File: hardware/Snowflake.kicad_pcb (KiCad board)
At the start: 2 copper layers, 58 parts, among them U1 556, U2 Mux_1_of_8

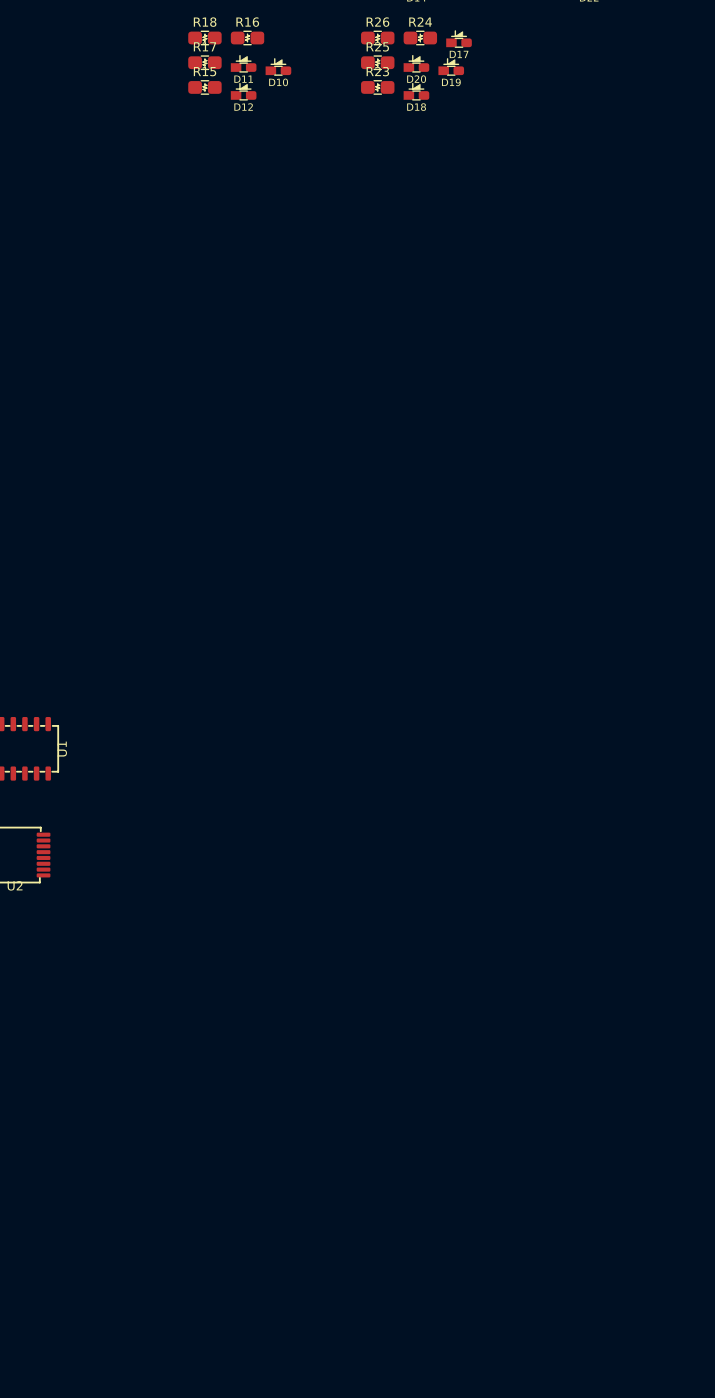
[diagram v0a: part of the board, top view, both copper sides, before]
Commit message: Added the Snowflake part to the library
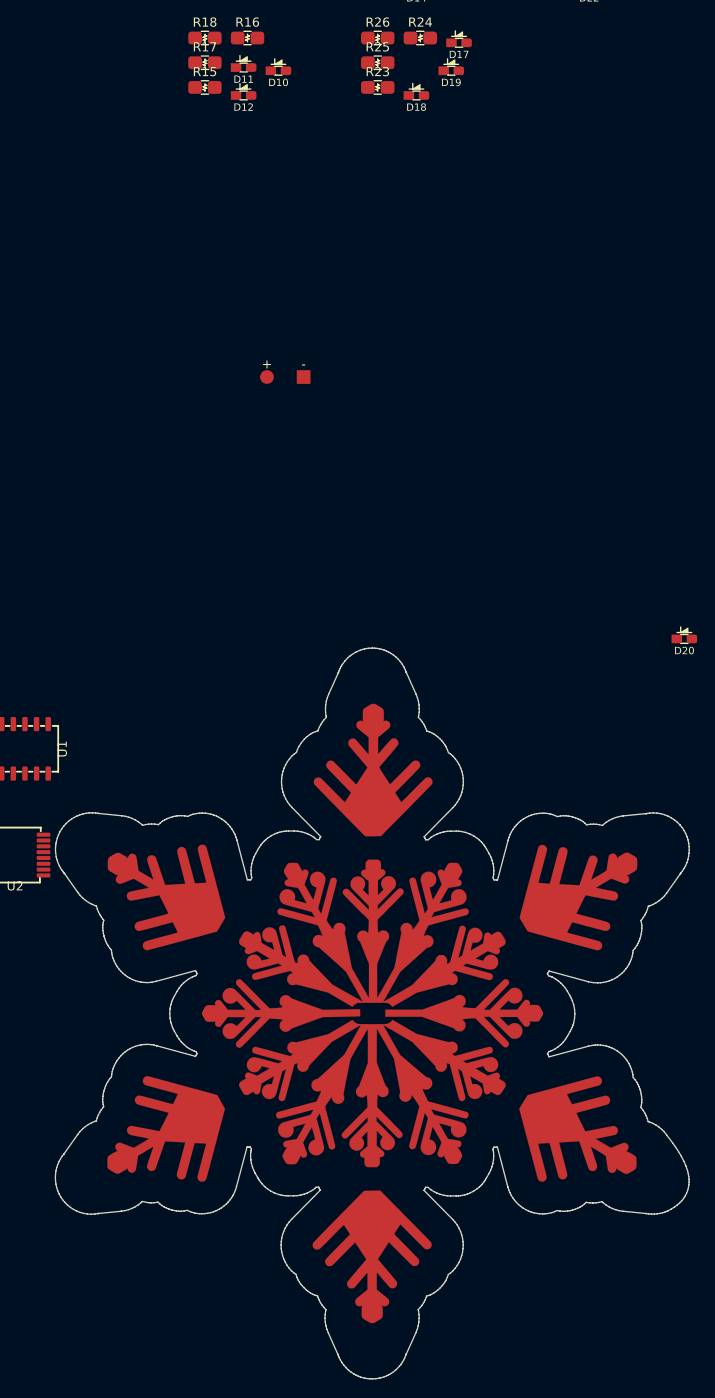
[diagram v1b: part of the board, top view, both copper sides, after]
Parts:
- added REF**: Battery_Holder-AAA, Snowflake:Battery_Holder-AAA, F.Cu at (119.8, 23.5)
- added Ref**: Val**, SnowFlake_1:Proto1, F.Cu at (129.3, 93.0)
- moved D20 68.9 mm to (163.4, 52.1)
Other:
- board outline added: 69.2 x 79.8 mm

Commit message: Schematic 99%, just needs a couple of tweaks (assign footprints to the OpAmp and the switch) Added a bunch of 3D models and footprints
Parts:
- removed C1, C2: C_Small, Snowflake:0805-C_Handsolder
- removed D1, D10, D11, D12, D13, D14, D15, D16, D17, D18, D19, D2, D20, D21, D22, D23, D24, D3, D4, D5, D6, D7, D8, D9: White, Snowflake:0603_LED_HandSolder
- removed R1, R2, R3, R4, R5, R6: R_Small, Snowflake:0805-R_Handsolder
- removed R10, R11, R12, R13, R14, R15, R16, R17, R18, R19, R20, R21, R22, R23, R24, R25, R26, R27, R28, R29, R30, R7, R8, R9: XYZΩ, Snowflake:0805-R_Handsolder
- removed REF**: Battery_Holder-AAA, Snowflake:Battery_Holder-AAA
- removed Ref**: Val**, SnowFlake_1:Proto1
- removed U1: 556, Snowflake:14-SOIC_4x8.75mm_.5-NA556
- removed U2: Mux_1_of_8, Snowflake:16-TSSOP_5x6.5mm_P0.65-MUX
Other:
- board outline removed

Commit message: Terayza new parts added and some layout started
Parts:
- added BT1: Battery, Snowflake:Battery_Holder-AAA, B.Cu at (206.8, 96.4)
- added C1: C_Small, Snowflake:0805-C_Handsolder, B.Cu at (162.0, 100.5)
- added D1: White, Snowflake:0603_LED_HandSolder, F.Cu at (108.6, 76.9)
- added D10: White, Snowflake:0603_LED_HandSolder, F.Cu at (138.2, 112.5)
- added D13: White, Snowflake:0603_LED_HandSolder, F.Cu at (108.5, 113.0)
- added D14: White, Snowflake:0603_LED_HandSolder, F.Cu at (108.5, 129.9)
- added D17: White, Snowflake:0603_LED_HandSolder, F.Cu at (93.1, 103.9)
- added D18: White, Snowflake:0603_LED_HandSolder, F.Cu at (78.8, 112.4)
- added D2: White, Snowflake:0603_LED_HandSolder, F.Cu at (108.5, 59.9)
- added D21: White, Snowflake:0603_LED_HandSolder, F.Cu at (92.5, 85.3)
- added D22: White, Snowflake:0603_LED_HandSolder, F.Cu at (77.6, 76.8)
- added D3: White, Snowflake:0603_LED_HandSolder, F.Cu at (108.5, 94.9)
- added D5: White, Snowflake:0603_LED_HandSolder, F.Cu at (123.9, 85.9)
- added D6: White, Snowflake:0603_LED_HandSolder, F.Cu at (138.4, 77.3)
- added D9: White, Snowflake:0603_LED_HandSolder, F.Cu at (123.7, 104.1)
- added Logo1: Snowflake, Snowflake:Snowflake, F.Cu at (108.5, 94.9)
- added R1: 50kΩ, Snowflake:0805-R_Handsolder, B.Cu at (159.4, 100.5)
- added R11: XYZΩ, Snowflake:0805-R_Handsolder, B.Cu at (139.5, 95.6)
- added R12: XYZΩ, Snowflake:0805-R_Handsolder, B.Cu at (143.5, 94.1)
- added R15: XYZΩ, Snowflake:0805-R_Handsolder, B.Cu at (123.1, 122.5)
- added R16: XYZΩ, Snowflake:0805-R_Handsolder, B.Cu at (126.4, 125.3)
- added R19: XYZΩ, Snowflake:0805-R_Handsolder, B.Cu at (92.2, 121.9)
- added R2: 35kΩ, Snowflake:0805-R_Handsolder, B.Cu at (156.1, 107.0)
- added R20: XYZΩ, Snowflake:0805-R_Handsolder, B.Cu at (91.5, 126.1)
- added R23: XYZΩ, Snowflake:0805-R_Handsolder, B.Cu at (76.9, 94.7)
- added R24: XYZΩ, Snowflake:0805-R_Handsolder, B.Cu at (72.9, 96.1)
- added R27: XYZΩ, Snowflake:0805-R_Handsolder, B.Cu at (93.1, 67.0)
- added R28: XYZΩ, Snowflake:0805-R_Handsolder, B.Cu at (89.8, 64.2)
- added R3: 30kΩ, Snowflake:0805-R_Handsolder, B.Cu at (166.6, 109.0)
- added R4: XYZΩ, Snowflake:0805-R_Handsolder, B.Cu at (163.0, 74.2)
- added R7: XYZΩ, Snowflake:0805-R_Handsolder, B.Cu at (124.8, 68.2)
- added R8: XYZΩ, Snowflake:0805-R_Handsolder, B.Cu at (125.5, 64.0)
- added RV1: 200kΩ, Snowflake:Potentiometer_TC33X-2-204E, B.Cu at (166.4, 104.2)
- added SW1: SW_SPST, Snowflake:Slide_Switch_JS202011SCQN, B.Cu at (167.8, 87.5)
- added U1: Opamp_Single, Snowflake:Op_Amp_SOT23_MCP6001T, B.Cu at (160.8, 107.5)
- added U2: 74HC595, Snowflake:16-TSSOP_5x6.5mm_P0.65-74HC565, B.Cu at (171.7, 76.1)
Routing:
- net Net-(R1-Pad2): track 0.00 -> 12.5 mm
- net Net-(R2-Pad2): track 0.00 -> 11.0 mm
- net CLK: track 0.00 -> 8.30 mm
- net Net-(C1-Pad1): track 0.00 -> 8.13 mm
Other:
- board outline added: 70.5 x 79.8 mm

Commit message: Terayza changes
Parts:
- added R5: 6.8kΩ, Snowflake:0805-R_Handsolder, B.Cu at (65.0, 96.1)
- added U3: LM4041_1.2V, Snowflake:SOT-23_LM4041_1.2V_Handsolder, B.Cu at (69.0, 97.2)
- moved U2 124.3 mm to (49.4, 98.2)
- moved R3 105.2 mm to (62.1, 96.1), turned to 90 degrees
- moved U1 103.5 mm to (57.6, 98.8)
- moved R1 102.3 mm to (57.5, 91.3), turned to 0 degrees
- moved RV1 100.8 mm to (66.4, 91.3), turned to 270 degrees
- moved R2 99.4 mm to (57.5, 94.0), turned to 0 degrees
- moved C1 88.5 mm to (73.6, 96.0)
- moved R4 53.4 mm to (113.8, 95.0), turned to 180 degrees
- moved SW1 22.0 mm to (152.2, 103.2)
- moved BT1 20.9 mm to (186.1, 99.3)
- moved R27 17.7 mm to (89.8, 84.3), turned to 150 degrees
- moved R15 17.3 mm to (127.2, 105.7), turned to 330 degrees
- moved R12 17.2 mm to (135.1, 79.2), turned to 210 degrees
- moved R28 17.1 mm to (81.7, 79.3), turned to 330 degrees
- moved R23 17.1 mm to (90.0, 105.8), turned to 210 degrees
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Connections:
- C1 pad 2: GND -> VBIAS
- R11 pad 2: GND -> /Stem 2/VK
- R12 pad 2: GND -> /Stem 2/VK
- R15 pad 2: GND -> /Stem 3/VK
- R16 pad 2: GND -> /Stem 3/VK
- R19 pad 2: GND -> /Stem 4/VK
- R20 pad 2: GND -> /Stem 4/VK
- R23 pad 2: GND -> /Stem 5/VK
- R24 pad 2: GND -> /Stem 5/VK
- R27 pad 2: GND -> /Stem 6/VK
- R28 pad 2: GND -> /Stem 6/VK
- R3 pad 2: GND -> VBIAS
- R7 pad 2: GND -> /Led Stem 1/VK
- R8 pad 2: GND -> /Led Stem 1/VK
- U1 pad 3: Net-(C1-Pad1) -> Net-(R2-Pad2)
- U1 pad 4: Net-(R2-Pad2) -> Net-(C1-Pad1)
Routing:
- net Net-(C1-Pad1): track 8.13 -> 30.8 mm
- net VBIAS: track 0.00 -> 13.0 mm
- net Net-(R1-Pad2): track 12.5 -> 6.22 mm
- net VBAT: track 0.00 -> 4.28 mm
- net Net-(R2-Pad2): track 11.0 -> 6.77 mm
- net CLK: track 8.30 -> 10.9 mm

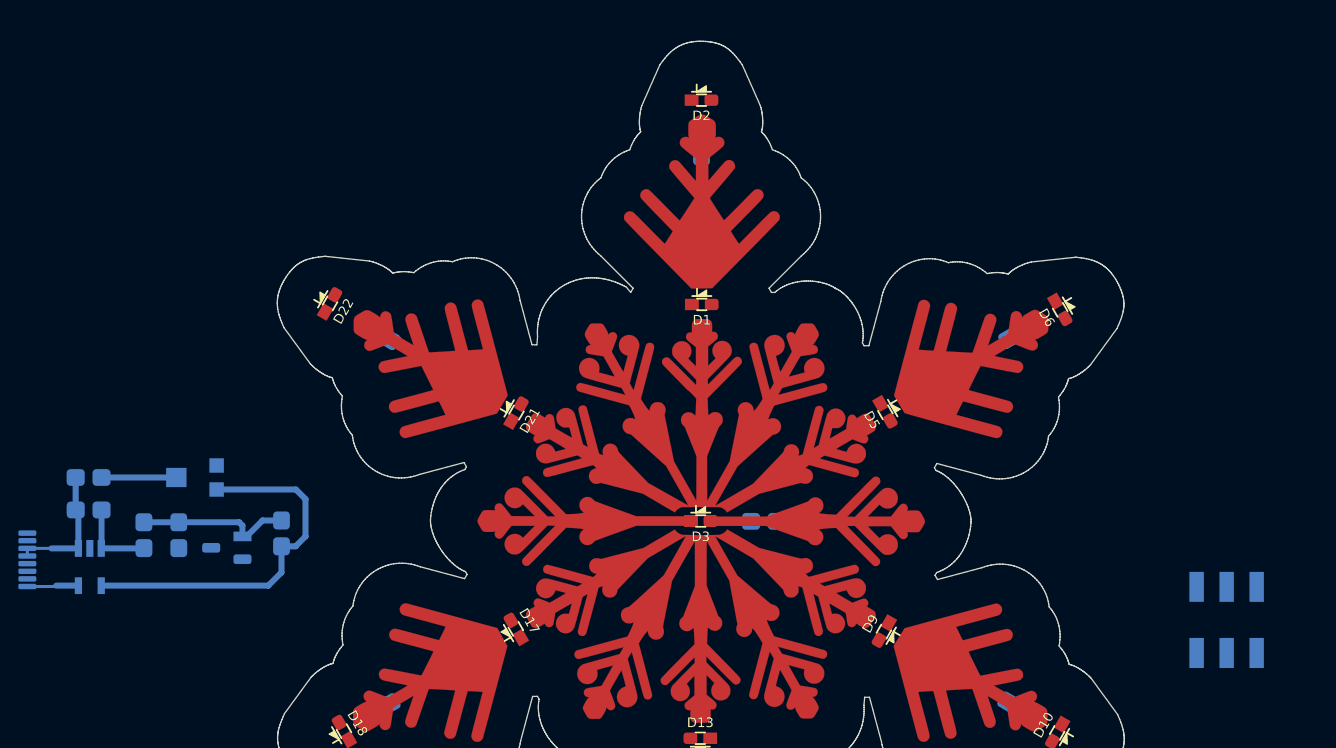
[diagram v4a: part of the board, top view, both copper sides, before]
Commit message: All footprints in place, schematic done
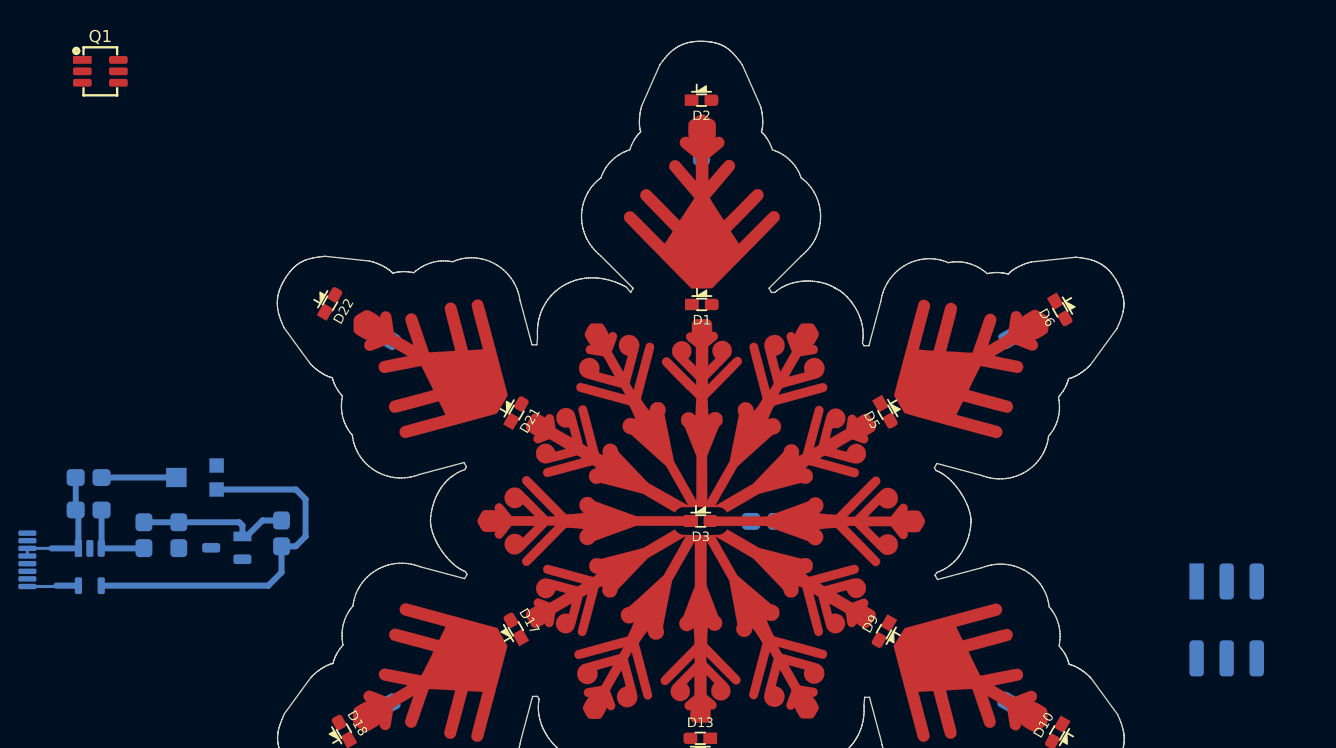
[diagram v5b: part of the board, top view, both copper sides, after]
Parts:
- added Q1: Q_DUAL_NMOS, Snowflake:SOT-23-6_DMN2004DMK_Handsoldering, F.Cu at (58.5, 57.5)
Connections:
- D1 pad A: ROW0 -> VBAT
- D10 pad A: RESET -> VBAT
- D13 pad A: ROW0 -> VBAT
- D14 pad A: RESET -> VBAT
- D17 pad A: ROW0 -> VBAT
- D18 pad A: RESET -> VBAT
- D2 pad A: RESET -> VBAT
- D21 pad A: ROW0 -> VBAT
- D22 pad A: RESET -> VBAT
- D5 pad A: ROW0 -> VBAT
- D6 pad A: RESET -> VBAT
- D9 pad A: ROW0 -> VBAT
- R11 pad 2: /Stem 2/VK -> ROW0
- R12 pad 2: /Stem 2/VK -> ROW1
- R15 pad 2: /Stem 3/VK -> ROW0
- R16 pad 2: /Stem 3/VK -> ROW1
- R19 pad 2: /Stem 4/VK -> ROW0
- R20 pad 2: /Stem 4/VK -> ROW1
- R23 pad 2: /Stem 5/VK -> ROW0
- R24 pad 2: /Stem 5/VK -> ROW1
- R27 pad 2: /Stem 6/VK -> ROW0
- R28 pad 2: /Stem 6/VK -> ROW1
- R7 pad 2: /Led Stem 1/VK -> ROW0
- R8 pad 2: /Led Stem 1/VK -> ROW1
- U2 pad 10: (no net) -> DRIVE_ROW1
- U2 pad 13: (no net) -> GND
- U2 pad 2: ROW0 -> DRIVE_ROW0
- U2 pad 3: RESET -> DRIVE_ROW1
- U3 pad 3: GND -> (no net)

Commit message: Still leaft to connect: Vbat from all the LEDs
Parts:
- Q1: moved to B.Cu
- moved BT1 99.4 mm to (89.5, 76.0), turned to 330 degrees
- moved Q1 74.6 mm to (120.3, 99.3)
- moved U2 71.4 mm to (120.5, 92.8), turned to 180 degrees
- moved SW1 70.8 mm to (85.0, 80.9), turned to 330 degrees
- moved R1 55.4 mm to (112.3, 99.6), turned to 180 degrees
- moved U1 54.9 mm to (112.2, 92.2), turned to 180 degrees
- moved R2 54.8 mm to (112.3, 96.9), turned to 180 degrees
- moved R3 45.6 mm to (107.7, 94.8), turned to 270 degrees
- moved R5 39.8 mm to (104.8, 94.8), turned to 270 degrees
- moved RV1 37.9 mm to (103.3, 99.6), turned to 90 degrees
- moved U3 31.9 mm to (100.8, 93.8), turned to 0 degrees
- moved C1 22.7 mm to (96.2, 95.0), turned to 270 degrees
- moved R4 14.5 mm to (128.2, 95.2), turned to 270 degrees
- moved R28 4.72 mm to (80.0, 74.9)
- moved R27 3.48 mm to (93.3, 84.3), turned to 330 degrees
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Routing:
- net ROW1: track 0.00 -> 201.5 mm
- net ROW0: track 0.00 -> 135.7 mm
- net VBAT: track 4.28 -> 36.3 mm, vias 0 -> 12
- net V1: track 0.00 -> 23.2 mm, vias 0 -> 1
- net GND: track 0.00 -> 20.5 mm, vias 0 -> 1
- net DRIVE_ROW1: track 0.00 -> 14.6 mm
- net DRIVE_ROW0: track 0.00 -> 13.3 mm
- net Net-(D22-PadK): track 0.00 -> 7.27 mm, vias 0 -> 1
- net LED0: track 0.00 -> 6.95 mm
- net Net-(D1-PadK): track 0.00 -> 5.21 mm, vias 0 -> 1
- net Net-(D10-PadK): track 0.00 -> 4.73 mm, vias 0 -> 1
- net Net-(D5-PadK): track 0.00 -> 4.59 mm, vias 0 -> 1
- net Net-(D13-PadK): track 0.00 -> 4.46 mm, vias 0 -> 1
- net Net-(D18-PadK): track 0.00 -> 4.34 mm, vias 0 -> 1
- net Net-(D9-PadK): track 0.00 -> 4.34 mm, vias 0 -> 1
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- added copper zone on B.Cu, net GND

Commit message: A bit of tidying up in the PCB.
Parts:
- added H1: MountingHole, Snowflake:MountingHole_2.1mm_M2, F.Cu at (108.5, 57.4)
- added R6: 0, Snowflake:0805-R_Handsolder, B.Cu at (116.8, 103.4)
- moved SW1 23.3 mm to (108.0, 84.7), turned to 0 degrees
- moved BT1 14.7 mm to (99.3, 87.0), turned to 0 degrees
- moved R28 5.81 mm to (82.9, 80.0)
- moved R27 4.73 mm to (88.6, 83.3), turned to 150 degrees
- moved R23 0.97 mm to (88.6, 106.5)
- moved R15 0.96 mm to (128.2, 106.7)
- moved R16 0.58 mm to (134.0, 110.1)
- moved R11 0.54 mm to (128.4, 83.3)
- moved R7 0.41 mm to (108.5, 71.7)
- moved D18 0.38 mm to (78.4, 112.4)
- moved R24 0.29 mm to (82.8, 109.8)
- moved D10 0.26 mm to (138.4, 112.6)
- moved D2 0.26 mm to (108.5, 60.0)
- moved R8 0.25 mm to (108.5, 65.0)
- moved R12 0.18 mm to (134.1, 79.9)
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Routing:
- net ROW1: track 201.5 -> 182.3 mm
- net ROW0: track 135.7 -> 152.0 mm
- net Net-(BT1-Pad1): track 3.57 -> 14.2 mm
- net VBAT: track 36.3 -> 26.9 mm, vias 12 -> 2
- net Net-(D22-PadK): track 7.27 -> 0.00 mm, vias 1 -> 0
- net Net-(D1-PadK): track 5.21 -> 0.17 mm, vias 1 -> 0
- net Net-(D10-PadK): track 4.73 -> 0.00 mm, vias 1 -> 0
- net Net-(D5-PadK): track 4.59 -> 0.00 mm, vias 1 -> 0
- net Net-(D13-PadK): track 4.46 -> 0.00 mm, vias 1 -> 0
- net Net-(D18-PadK): track 4.34 -> 0.00 mm, vias 1 -> 0
- net Net-(D9-PadK): track 4.34 -> 0.00 mm, vias 1 -> 0
- net Net-(D14-PadK): track 4.33 -> 0.00 mm, vias 1 -> 0
- net Net-(D17-PadK): track 4.32 -> 0.00 mm, vias 1 -> 0
- net Net-(D2-PadK): track 4.21 -> 0.00 mm, vias 1 -> 0
- net Net-(D6-PadK): track 4.19 -> 0.00 mm, vias 1 -> 0
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- added copper zone on F.Cu, net VBAT

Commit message: Test
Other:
- board text added: "DRC: Can't internally connect this pins"
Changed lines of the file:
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@@
   (general
     (thickness 1.6)
-    (drawings 3)
+    (drawings 5)
     (tracks 149)
     (zones 0)
@@
   (page A4)
   (layers
-    (0 F.Cu signal)
+    (0 F.Cu signal hide)
     (31 B.Cu signal)
     (32 B.Adhes user)
@@
   )
   (setup
-    (last_trace_width 0.5)
+    (last_trace_width 0.25)
     (user_trace_width 0.25)
     (user_trace_width 0.5)
@@
     (pad "" np_thru_hole circle (at 0 0) (size 2.1 2.1) (drill 2.1) (layers *.Cu *.Mask))
   )
+  (gr_text "DRC: Can't internally \nconnect this pins" (at 106.7 84.6) (layer Eco1.User)
+    (effects (font (size 0.25 0.25) (thickness 0.0625)))
+  )
+  (gr_text "DRC: Can't internally \nconnect this pins" (at 119.8 105) (layer Eco1.User)
+    (effects (font (size 0.25 0.25) (thickness 0.0625)))
+  )
   (gr_line (start 85.74 106.01) (end 102.04 115.41) (layer Eco1.User) (width 0.12))
